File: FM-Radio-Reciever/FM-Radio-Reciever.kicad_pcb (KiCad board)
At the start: 4 copper layers, 73 x 73 mm, 214 parts, among them J1 ANT-IN, J2 GND, J4 10.7MHz Filter, J5 GND, J6 MPX-OUT, J7 +5V, J8 GND, Q1 2SK3557, Q10 MMDT3904, Q11 MMDT3904, Q12 MMBT3904, Q13 MMDT3904, Q14 MMDT3904, Q15 MMDT3904, Q16 MMBT3904, Q2 2SK3557, Q3 2SK3557, Q4 2SK3557, Q5 2SK3557, Q6 MMBT3904, Q7 MMDT3904, Q8 MMDT3904, Q9 MMDT3904, SW1 AFC_SW, T1 2.21u, T2 IFT_7mmx7mm, U1 LM393

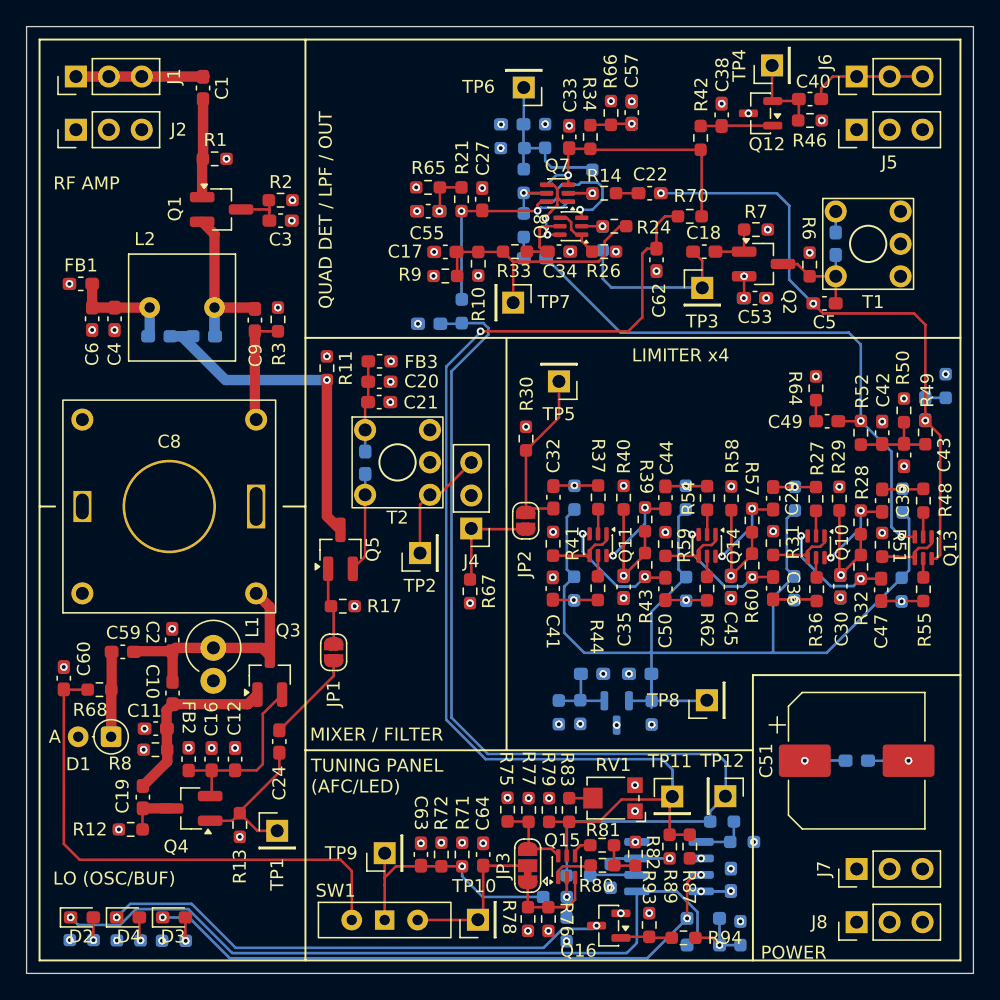
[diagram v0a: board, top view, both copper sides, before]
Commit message: PVCとIFTのフットプリント調整
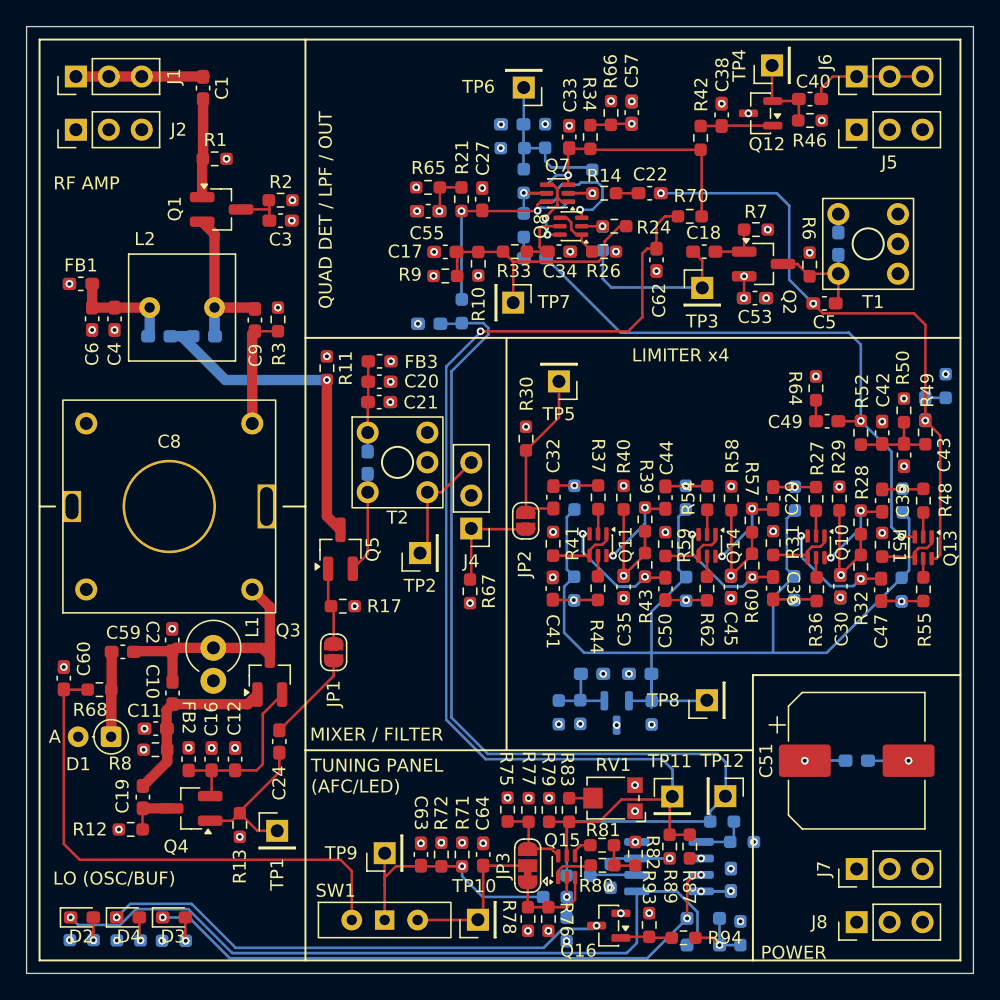
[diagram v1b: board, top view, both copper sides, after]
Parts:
- T2: value IFT_7mmx7mm -> IFT_7mm
- moved C13 0.20 mm to (162.6, 116.7)
- moved C25 0.18 mm to (126.3, 133.6)
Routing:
- net Net-(Q8B-C2): track 9.63 -> 9.12 mm
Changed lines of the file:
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@@
 		(sheetname "/")
 		(sheetfile "FM-Radio-Reciever.kicad_sch")
-		(units
-			(unit
-				(name "A")
-				(pins "1" "2" "5" "4" "3")
-			)
-		)
 		(attr through_hole)
 		(duplicate_pad_numbers_are_jumpers no)
@@
 		(fp_circle
 			(center 0 0)
-			(end 1.4 0)
+			(end 1.2 0)
 			(stroke
 				(width 0.15)
@@
 		)
 		(pad "1" thru_hole circle
-			(at -2.5 -2.5)
+			(at -2.3 -2.3)
 			(size 1.7 1.7)
 			(drill 1)
@@
 		)
 		(pad "2" thru_hole circle
-			(at -2.5 2.5)
+			(at -2.3 2.3)
 			(size 1.7 1.7)
 			(drill 1)
@@
 		)
 		(pad "3" thru_hole circle
-			(at 2.5 -2.5)
+			(at 2.3 -2.3)
 			(size 1.7 1.7)
 			(drill 1)
@@
 		)
 		(pad "4" thru_hole circle
-			(at 2.5 0)
+			(at 2.3 0)
 			(size 1.7 1.7)
 			(drill 1)
@@
 		)
 		(pad "5" thru_hole circle
-			(at 2.5 2.5)
+			(at 2.3 2.3)
 			(size 1.7 1.7)
 			(drill 1)
@@
 		(sheetname "/")
 		(sheetfile "FM-Radio-Reciever.kicad_sch")
-		(units
-			(unit
-				(name "A")
-				(pins "3" "5" "1" "2")
-			)
-			(unit
-				(name "B")
-				(pins "4" "5" "1-UB" "2-UB")
-			)
-		)
 		(attr through_hole)
 		(duplicate_pad_numbers_are_jumpers no)
@@
 		)
 		(pad "1" thru_hole circle
-			(at -6.7 -6.7 90)
+			(at -6.4 -6.4 90)
 			(size 1.7 1.7)
 			(drill 1)
@@
 		)
 		(pad "2" thru_hole circle
-			(at 6.7 -6.7 90)
+			(at 6.4 -6.4 90)
 			(size 1.7 1.7)
 			(drill 1)
@@
 		)
 		(pad "3" thru_hole circle
-			(at -6.7 6.7 90)
+			(at -6.4 6.4 90)
 			(size 1.7 1.7)
 			(drill 1)
@@
 		)
 		(pad "4" thru_hole circle
-			(at 6.7 6.7 90)
+			(at 6.4 6.4 90)
 			(size 1.7 1.7)
 			(drill 1)
@@
 		)
 		(pad "5" thru_hole rect
-			(at 0 -6.7 90)
+			(at 0 -7.5 90)
 			(size 2.4 1.4)
 			(drill oval 2 1)
@@
 		)
 		(pad "5" thru_hole rect
-			(at 0 6.7 90)
+			(at 0 7.5 90)
 			(size 3.4 1.4)
 			(drill oval 3 1)
@@
 			)
 		)
-		(property "Value" "IFT_7mmx7mm"
+		(property "Value" "IFT_7mm"
 			(at 0 4.5 0)
 			(layer "F.Fab")
@@
 		(sheetname "/")
 		(sheetfile "FM-Radio-Reciever.kicad_sch")
-		(units
-			(unit
-				(name "A")
-				(pins "1" "2" "5" "4" "3")
-			)
-		)
 		(attr through_hole)
 		(duplicate_pad_numbers_are_jumpers no)
@@
 		(fp_circle
 			(center 0 0)
-			(end 1.4 0)
+			(end 1.2 0)
 			(stroke
 				(width 0.15)
@@
 		)
 		(pad "1" thru_hole circle
-			(at -2.5 -2.5)
+			(at -2.3 -2.3)
 			(size 1.7 1.7)
 			(drill 1)
@@
 		)
 		(pad "2" thru_hole circle
-			(at -2.5 2.5)
+			(at -2.3 2.3)
 			(size 1.7 1.7)
 			(drill 1)
@@
 		)
 		(pad "3" thru_hole circle
-			(at 2.5 -2.5)
+			(at 2.3 -2.3)
 			(size 1.7 1.7)
 			(drill 1)
@@
 		)
 		(pad "4" thru_hole circle
-			(at 2.5 0)
+			(at 2.3 0)
 			(size 1.7 1.7)
 			(drill 1)
@@
 		)
 		(pad "5" thru_hole circle
-			(at 2.5 2.5)
+			(at 2.3 2.3)
 			(size 1.7 1.7)
 			(drill 1)
@@
 	(footprint "Capacitor_SMD:C_0603_1608Metric_Pad1.08x0.95mm_HandSolder"
 		(layer "B.Cu")
-		(at 162.3822 116.7433 -90)
+		(at 162.5854 116.7373 -90)
 		(descr "Capacitor SMD 0603 (1608 Metric), square (rectangular) end terminal, IPC-7351 nominal with elongated pad for handsoldering. (Body size source: IPC-SM-782 page 76, https://www.pcb-3d.com/wordpress/wp-content/uploads/ipc-sm-782a_amendment_1_and_2.pdf)")
 		(tags "capacitor handsolder")
@@
 	(footprint "Capacitor_SMD:C_0603_1608Metric_Pad1.08x0.95mm_HandSolder"
 		(layer "B.Cu")
-		(at 126.111 133.6305 -90)
+		(at 126.2888 133.6283 -90)
 		(descr "Capacitor SMD 0603 (1608 Metric), square (rectangular) end terminal, IPC-7351 nominal with elongated pad for handsoldering. (Body size source: IPC-SM-782 page 76, https://www.pcb-3d.com/wordpress/wp-content/uploads/ipc-sm-782a_amendment_1_and_2.pdf)")
 		(tags "capacitor handsolder")
@@
 	)
 	(segment
-		(start 138.6605 167.8959)
-		(end 138.6586 167.894)
-		(width 0.2)
-		(layer "F.Cu")
-		(net "Net-(JP3-A)")
-	)
-	(segment
 		(start 141.711229 167.8959)
 		(end 140.2334 167.8959)
@@
 	)
 	(segment
-		(start 162.386 114.253)
-		(end 162.386 115.877)
+		(start 162.586 114.453)
+		(end 162.586 115.8742)
 		(width 0.2)
 		(layer "B.Cu")
@@
 	)
 	(segment
-		(start 126.1 131.1)
-		(end 126.1 129.173499)
+		(start 126.3 131.3)
+		(end 126.3 128.973499)
 		(width 0.2)
 		(layer "F.Cu")
@@
 	)
 	(segment
-		(start 126.1 131.1)
-		(end 126.1 132.757)
+		(start 126.2888 132.7658)
+		(end 126.2888 131.3112)
 		(width 0.2)
 		(layer "B.Cu")
@@
 	)
 	(segment
-		(start 162.386 119.253)
-		(end 162.386 121.3336)
+		(start 162.586 119.053)
+		(end 160.5794 119.053)
 		(width 0.2)
 		(layer "F.Cu")
@@
 	)
 	(segment
-		(start 159.4206 118.3018)
-		(end 160.3756 119.2568)
+		(start 162.586 119.053)
+		(end 162.586 121.1336)
 		(width 0.2)
 		(layer "F.Cu")
@@
 	)
 	(segment
-		(start 162.386 119.253)
-		(end 160.3794 119.253)
+		(start 159.4206 118.3018)
+		(end 160.3756 119.2568)
 		(width 0.2)
 		(layer "F.Cu")
@@
 	)
 	(segment
-		(start 162.386 119.253)
-		(end 162.386 117.6096)
+		(start 162.586 119.053)
+		(end 162.586 117.6004)
 		(width 0.2)
 		(layer "B.Cu")
@@
 	)
 	(segment
+		(start 117.4 123.6946)
+		(end 117.602 123.4926)
+		(width 0.8)
+		(layer "F.Cu")
+		(net "Net-(C8-Pad4)")
+	)
+	(segment
 		(start 117.602 123.4926)
 		(end 119.3784 123.4926)
@@
 	)
 	(segment
-		(start 117.602 123.4926)
-		(end 117.602 130.202)
+		(start 117.4 123.6946)
+		(end 117.4 130.6)
 		(width 0.8)
 		(layer "F.Cu")
@@
 	)
 	(segment
-		(start 138.684 161.2862)
-		(end 138.7094 161.3116)
-		(width 0.2)
-		(layer "F.Cu")
-		(net "Net-(JP3-B)")
-	)
-	(segment
 		(start 140.4514 163.3936)
 		(end 140.9908 163.933)
@@
 	)
 	(segment
-		(start 143.5904 112.8418)
-		(end 143.6224 112.8738)
-		(width 0.2)
-		(layer "B.Cu")
-		(net "Net-(Q7A-B1)")
-	)
-	(segment
 		(start 141.7709 112.8418)
 		(end 143.5904 112.8418)
@@
 	)
 	(segment
-		(start 117.7 143.7)
-		(end 118.75 144.75)
-		(width 0.8)
-		(layer "F.Cu")
-		(net "Net-(Q3-G)")
-	)
-	(segment
 		(start 118.1542 147.9042)
 		(end 114.4042 147.9042)
@@
 	)
 	(segment
+		(start 118.75 144.75)
+		(end 117.4 143.4)
+		(width 0.8)
+		(layer "F.Cu")
+		(net "Net-(Q3-G)")
+	)
+	(segment
 		(start 111.4848 147.9)
 		(end 111.252 148.1328)
@@
 	)
 	(segment
-		(start 126.1 140.85)
-		(end 126.1 136.1)
+		(start 126.3 140.65)
+		(end 126.3 135.9)
 		(width 0.2)
 		(layer "F.Cu")
@@
 	(segment
 		(start 125.15 141.8)
-		(end 126.1 140.85)
+		(end 126.3 140.65)
 		(width 0.2)
 		(layer "F.Cu")
@@
 	)
 	(segment
-		(start 126.111 134.493)
-		(end 126.111 136.089)
+		(start 126.2888 134.4908)
+		(end 126.2888 135.8888)
 		(width 0.2)
 		(layer "B.Cu")
@@
 	)
 	(segment
-		(start 130.335 140.591999)
-		(end 130.335 136.865)
+		(start 134.286822 133.6154)
+		(end 132.002222 135.9)
 		(width 0.2)
 		(layer "F.Cu")
@@
 	)
 	(segment
-		(start 130.335 136.865)
-		(end 131.1 136.1)
+		(start 130.9116 140.015399)
+		(end 130.9116 135.9116)
 		(width 0.2)
 		(layer "F.Cu")
@@
 	)
 	(segment
-		(start 134.286822 133.6154)
-		(end 131.802222 136.1)
+		(start 132.002222 135.9)
+		(end 130.9 135.9)
 		(width 0.2)
 		(layer "F.Cu")
@@
 	)
 	(segment
-		(start 143.6224 111.0488)
-		(end 143.4288 110.8552)
-		(width 0.2)
-		(layer "B.Cu")
-		(net "/VBU")
-	)
-	(segment
 		(start 138.3322 104.6988)
 		(end 138.3322 107.5182)
@@
 		(width 0.2)
 		(layer "B.Cu")
-		(net "Net-(Q8B-C2)")
-	)
-	(segment
-		(start 142.283399 112.1918)
-		(end 141.7709 112.1918)
-		(width 0.2)
-		(layer "B.Cu")

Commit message: プロトタイプ基板発注
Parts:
- T2: value IFT_7mm -> IFT_7mmx7mm
- moved D1 6.08 mm to (107.4, 148.7), turned to -90 degrees
- moved R68 4.81 mm to (106.6, 146.4)
- moved C60 3.81 mm to (103.0, 146.4), turned to 180 degrees
- moved C59 2.39 mm to (109.6, 147.3), turned to 90 degrees
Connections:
- net Net-(Q2-G) renamed /Q_TANK
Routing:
- net Net-(D1-K): track 6.51 -> 4.42 mm
- net Net-(Q3-G): track 18.8 -> 17.0 mm
- net /AFC_V: track 40.6 -> 42.0 mm
- net Net-(Q5-G): track 26.3 -> 25.2 mm
- net /DB: track 91.5 -> 90.5 mm
- net GND: vias 66 -> 191
- added copper zone on B.Cu, net GND
- added copper zone on F.Cu, net GND
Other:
- board text added: "FM-Radio-Reciever Proto 2026/10/18 Akira345"

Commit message: コンデンサの値間違い修正
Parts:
- C14: value 39p -> 33p
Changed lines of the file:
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@@
 			)
 		)
-		(property "Value" "39p"
+		(property "Value" "33p"
 			(at 0 -1.43 0)
 			(layer "B.Fab")
